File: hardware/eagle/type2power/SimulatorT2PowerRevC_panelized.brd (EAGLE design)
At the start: 48.3 x 48.3 mm, 7 parts

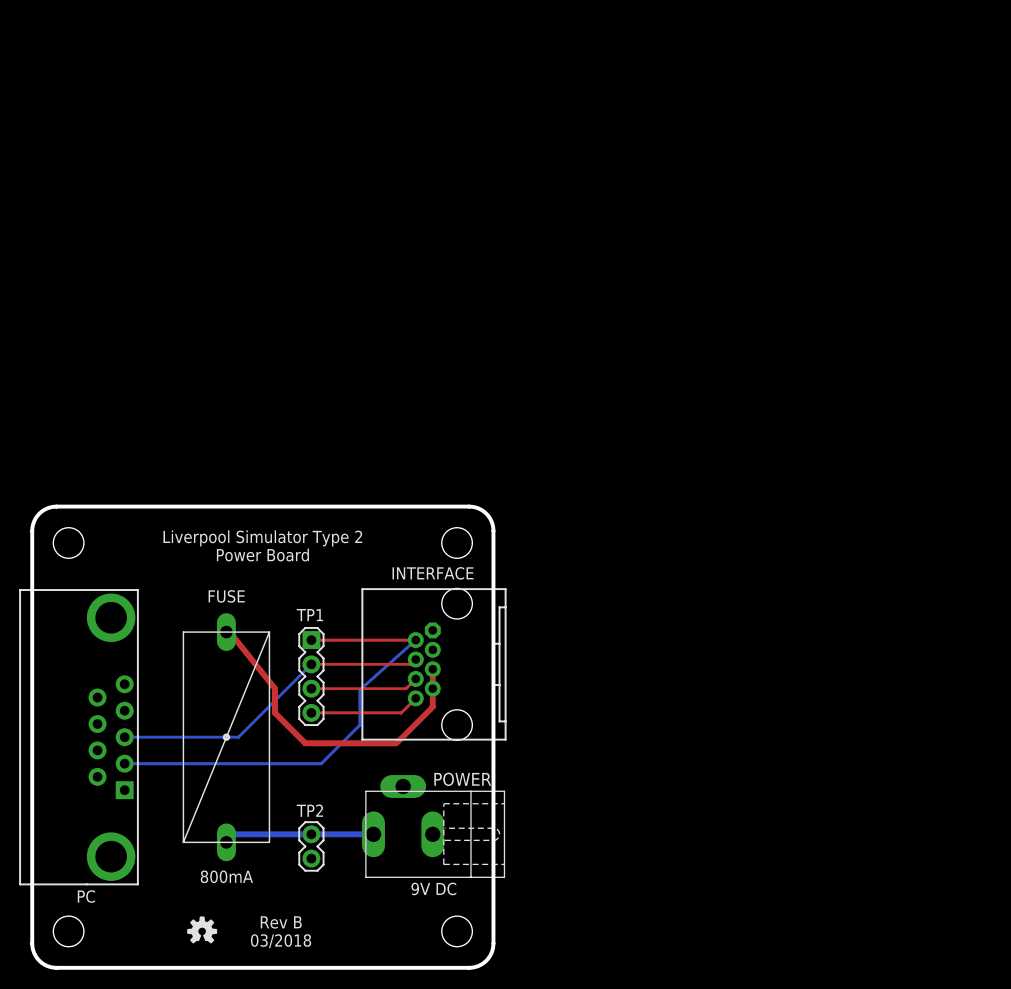
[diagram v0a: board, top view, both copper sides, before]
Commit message: Power Board Rev C
Add an indication of power supply polarity to the top silkscreen.
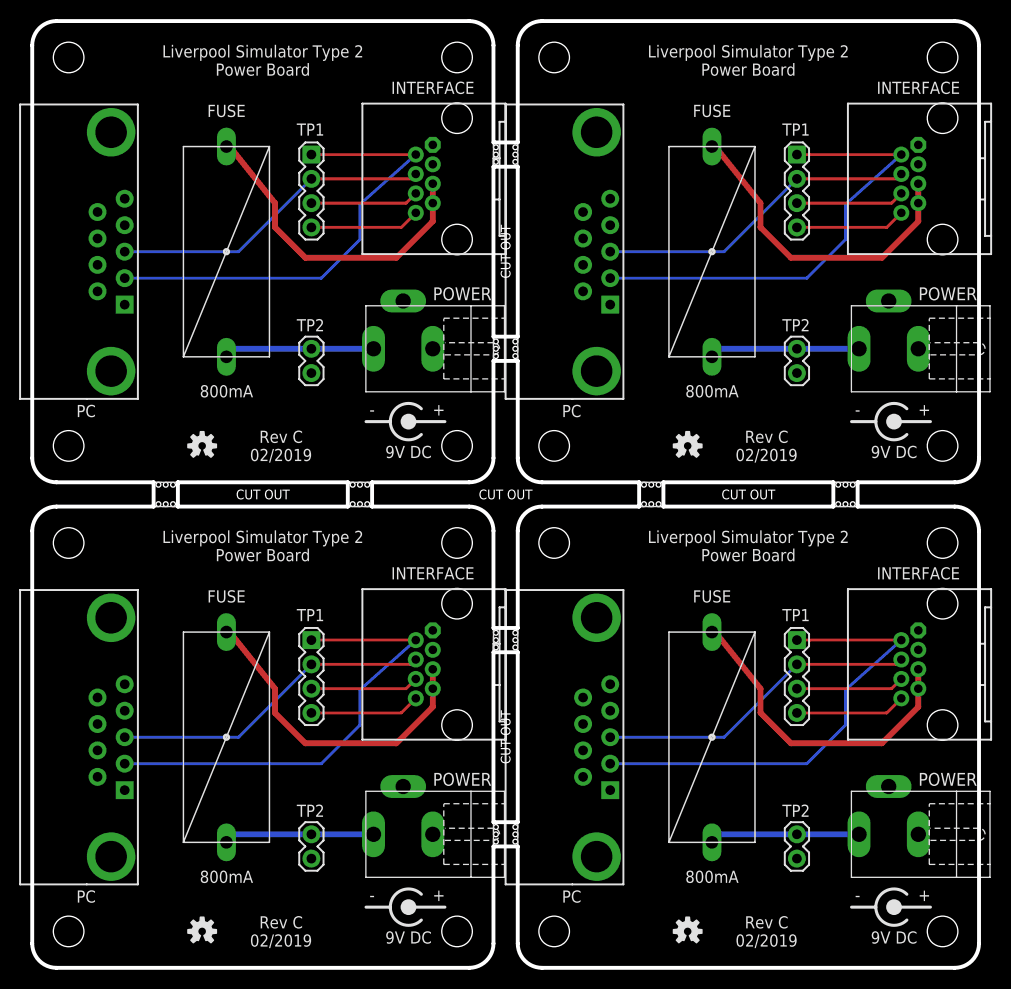
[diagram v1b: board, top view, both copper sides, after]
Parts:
- added E$1, E$2, E$3, E$4, E$5, E$6, E$7, E$8: (no value), AIC_Custom:STAMP_HOLES
- added FUSE_1, FUSE_2, FUSE_3: 800mA, AIC_Custom:MCOMP-FUSE-HOLDER-PCB
- added INTERFACE_1, INTERFACE_2, INTERFACE_3: RJ45-RJHSE-X08090DEG, AIC_Custom:RJ45-RJHSE-5080
- added LOGO1_1, LOGO1_2, LOGO1_3: OSHW-LOGOS, SparkFun-Aesthetics:OSHW-LOGO-S
- added PC_1, PC_2, PC_3: (no value), AIC_Custom:MULTICOMP-DB9-FEMALE-PCB-90DEG
- added POWER_1, POWER_2, POWER_3: 9V DC, AIC_Custom:CLIFF-FC681465P-DC-JACK
- added TP1_1, TP1_2, TP1_3: (no value), SparkFun-Connectors:1X04
- added TP2_1, TP2_2, TP2_3: (no value), SparkFun-Connectors:1X02
- added U$1, U$1_1, U$1_2, U$1_3: (no value), AIC_Custom:CENTRE-POS-SILK
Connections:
- net P6 renamed TX2
- new net GND1: INTERFACE_1.1, INTERFACE_1.3, PC_1.5, POWER_1.3, TP2_1.2
- new net GND2: INTERFACE_2.1, INTERFACE_2.3, PC_2.5, POWER_2.3, TP2_2.2
- new net GND3: INTERFACE_3.1, INTERFACE_3.3, PC_3.5, POWER_3.3, TP2_3.2
- new net P81: INTERFACE_1.8, TP1_1.4
- new net P82: INTERFACE_2.8, TP1_2.4
- new net P83: INTERFACE_3.8, TP1_3.4
- new net RXD1: INTERFACE_1.4, PC_1.3, TP1_1.2
- new net RXD2: INTERFACE_2.4, PC_2.3, TP1_2.2
- new net RXD3: INTERFACE_3.4, PC_3.3, TP1_3.2
- new net TX21: INTERFACE_1.6, TP1_1.3
- new net TX22: INTERFACE_2.6, TP1_2.3
- new net TX23: INTERFACE_3.6, TP1_3.3
- new net TXD1: INTERFACE_1.2, PC_1.2, TP1_1.1
- new net TXD2: INTERFACE_2.2, PC_2.2, TP1_2.1
- new net TXD3: INTERFACE_3.2, PC_3.2, TP1_3.1
- new net VIN1: FUSE_1.2, POWER_1.1, TP2_1.1
- new net VIN21: FUSE_1.1, INTERFACE_1.5, INTERFACE_1.7
- new net VIN22: FUSE_2.1, INTERFACE_2.5, INTERFACE_2.7
- new net VIN23: FUSE_3.1, INTERFACE_3.5, INTERFACE_3.7
- new net VIN3: FUSE_2.2, POWER_2.1, TP2_2.1
- new net VIN4: FUSE_3.2, POWER_3.1, TP2_3.1
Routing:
- net TXD3: track 0.00 -> 48.7 mm
- net TXD2: track 0.00 -> 48.7 mm
- net TXD1: track 0.00 -> 48.7 mm
- net VIN23: track 0.00 -> 34.4 mm
- net VIN22: track 0.00 -> 34.4 mm
- net VIN21: track 0.00 -> 34.4 mm
- net RXD3: track 0.00 -> 33.8 mm
- net RXD2: track 0.00 -> 33.8 mm
- net RXD1: track 0.00 -> 33.8 mm
- net VIN1: track 0.00 -> 15.9 mm
- net VIN4: track 0.00 -> 15.9 mm
- net VIN3: track 0.00 -> 15.9 mm
- net P83: track 0.00 -> 11.6 mm
- net P82: track 0.00 -> 11.6 mm
- net P81: track 0.00 -> 11.6 mm
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- added copper zone on layer 1, net GND1
- added copper zone on layer 16, net GND1
- added copper zone on layer 1, net GND2
- added copper zone on layer 16, net GND2
- added copper zone on layer 1, net GND3
- added copper zone on layer 16, net GND3
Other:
- board size 48.3 x 48.3 mm -> 99.1 x 99.1 mm
- board text added: "CUT OUT"
- board text added: "FUSE"
- board text added: "INTERFACE"
- board text added: "PC"
- board text added: "POWER"
- board text added: "Rev C 02/2019"
- board text added: "TP1"
- board text added: "TP2"
- board text removed: "Rev B 03/2018"
